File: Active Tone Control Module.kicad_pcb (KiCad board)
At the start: 2 copper layers, 30 parts, among them J1 Sound INPUT, J2 VCC, J3 Amplifier, U1 TL074

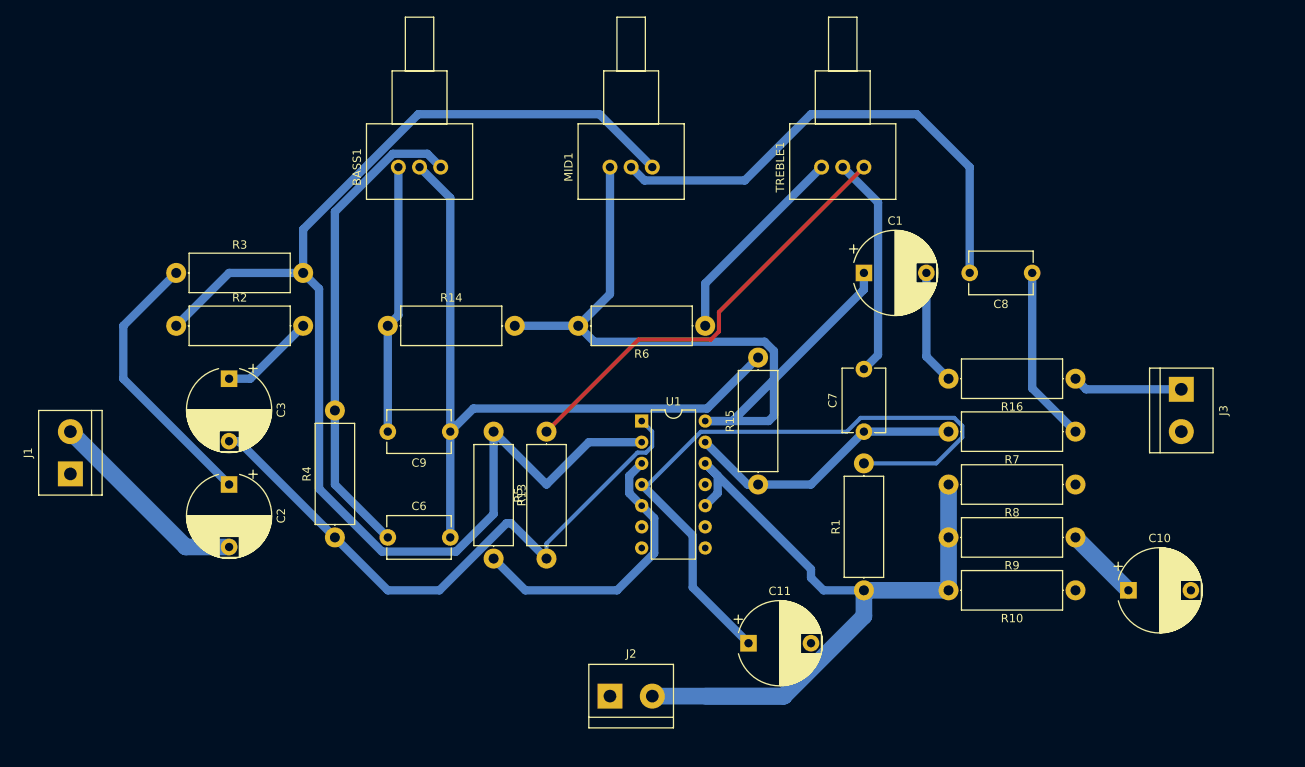
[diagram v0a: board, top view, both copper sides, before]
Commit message: Active Tone Control module is restored
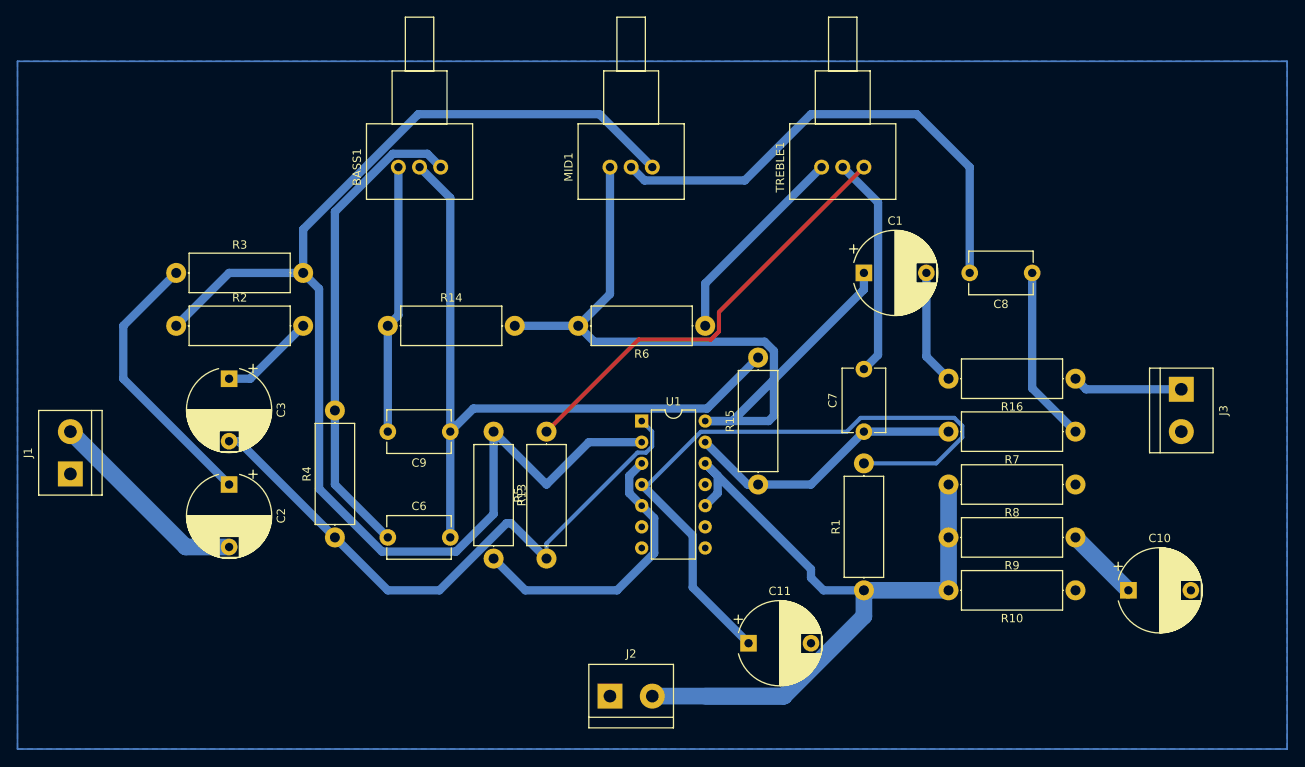
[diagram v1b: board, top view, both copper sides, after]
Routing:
- added copper zone on B.Cu, net Earth
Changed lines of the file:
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@@
       (sketchpadsonfab false)
       (subtractmaskfromsilk false)
-      (outputformat 1)
+      (outputformat 4)
       (mirror false)
-      (drillshape 1)
+      (drillshape 0)
       (scaleselection 1)
-      (outputdirectory "")
+      (outputdirectory "C:/Users/mitxar/Documents/uc3843/Active Tone Control Module/PCB drill pdf gerber/")
     )
   )
@@
     )
   )
+  (gr_rect (start 38.1 31.75) (end 190.5 114.3)
+    (stroke (width 0.2) (type default)) (fill none) (layer "B.Cu"))
   (segment (start 76.2 49.807258) (end 83.157258 42.85) (width 1) (layer "B.Cu") (net 1))
   (segment (start 76.2 82.55) (end 76.2 73.66) (width 1) (layer "B.Cu") (net 1))
@@
   (segment (start 95.25 91.44) (end 99.06 95.25) (width 1) (layer "B.Cu") (net 22))
   (segment (start 114.53 86.59) (end 113.03 85.09) (width 1) (layer "B.Cu") (net 22))
+  (zone (net 15) (net_name "Earth") (layer "B.Cu") (hatch edge 0.5)
+    (connect_pads (clearance 0.5))
+    (min_thickness 0.25) (filled_areas_thickness no)
+    (fill yes (thermal_gap 0.5) (thermal_bridge_width 0.5))
+    (polygon
+      (pts
+        (xy 38.1 31.75)
+        (xy 38.1 114.3)
+        (xy 190.5 114.3)
+        (xy 190.5 31.75)
+      )
+    )
+  )
 )
